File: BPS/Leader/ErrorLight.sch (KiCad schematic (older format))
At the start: 15 parts, among them J10 ErrorLightConn, Q3 NTR4003NT1G, Q4 VND5N07-E, U12 SI8261ABC-IS

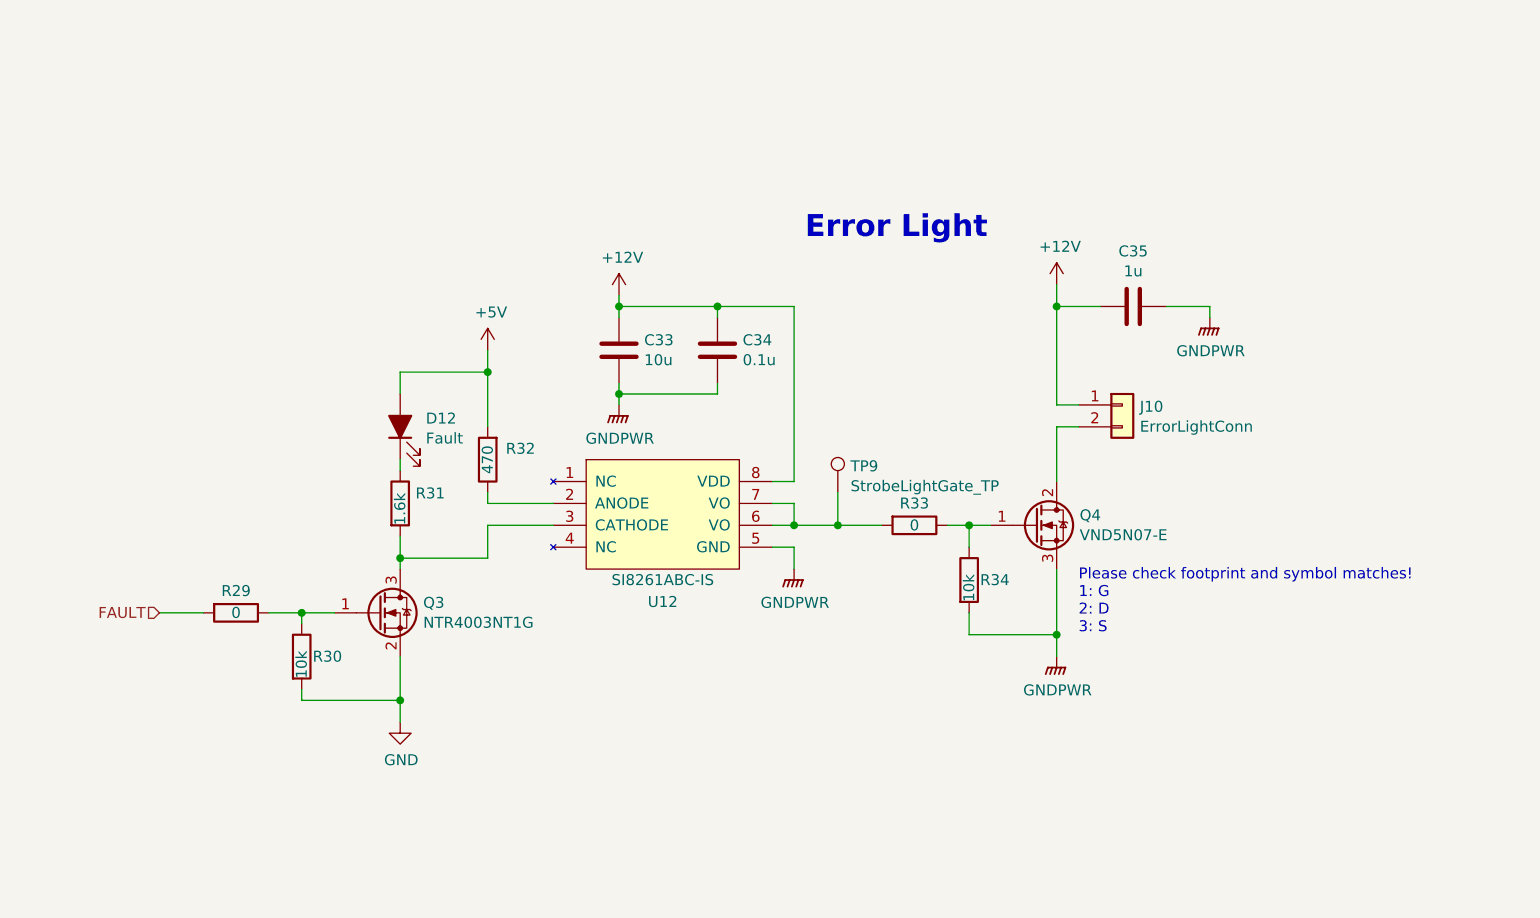
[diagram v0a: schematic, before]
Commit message: Places most components of leader board in their respective locations with nothing traced
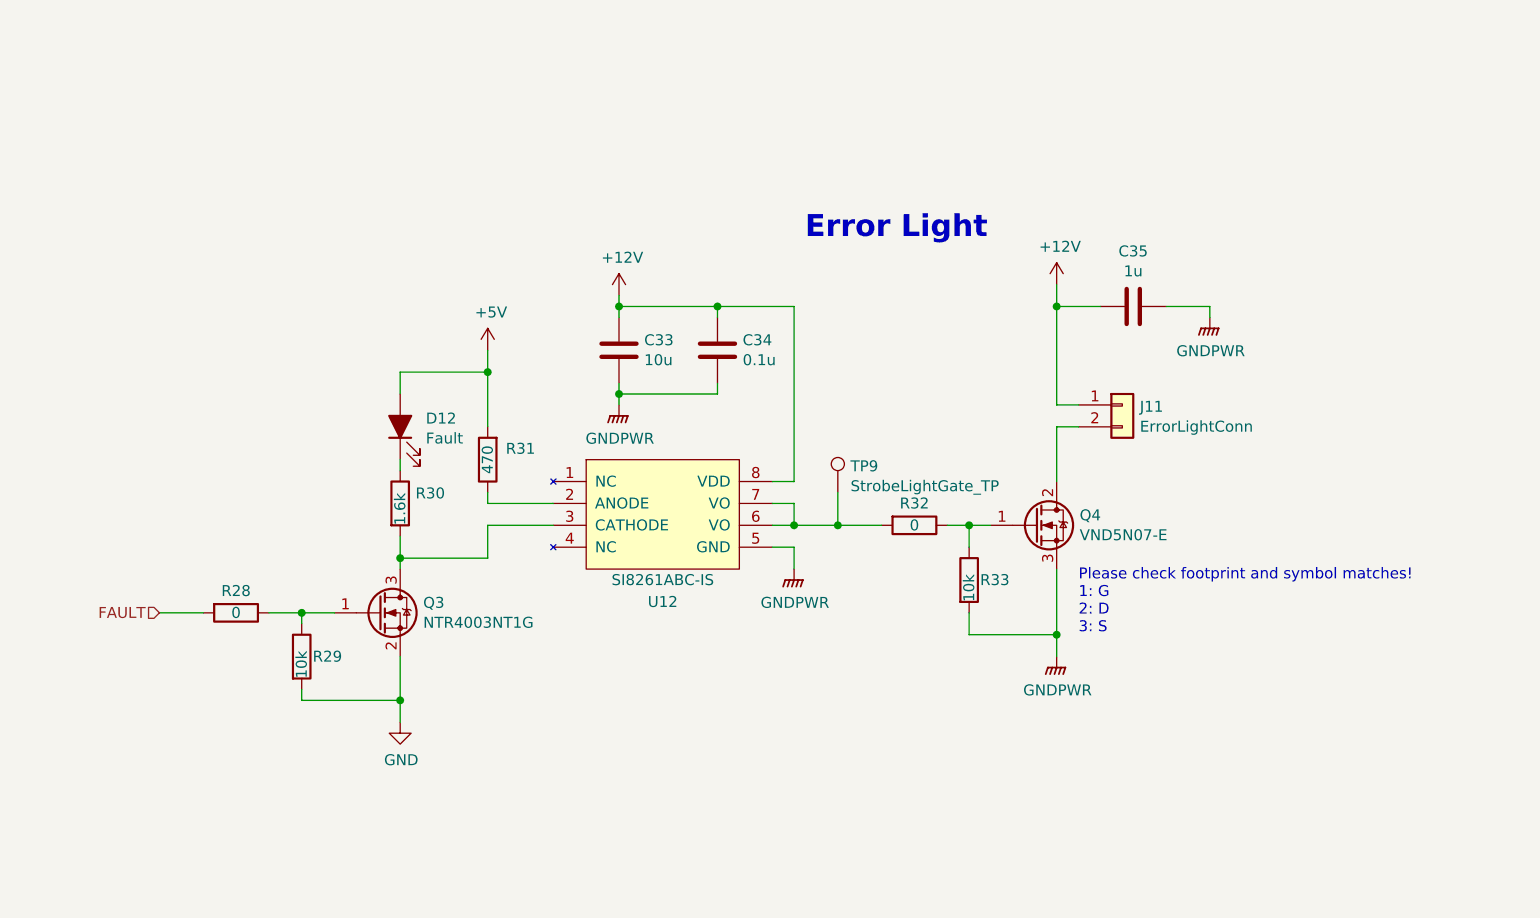
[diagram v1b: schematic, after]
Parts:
- renumbered J10 to J11, R29 to R28, R30 to R29, R31 to R30, R32 to R31, R33 to R32, R34 to R33
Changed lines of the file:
@@
 P 7350 3400
 AR Path="/5C392C6A/5D93093E" Ref="J?"  Part="1"
-AR Path="/5D923D59/5D93093E" Ref="J10"  Part="1"
-F 0 "J10" H 7430 3392 50  0000 L CNN
+AR Path="/5D923D59/5D93093E" Ref="J11"  Part="1"
+F 0 "J11" H 7430 3392 50  0000 L CNN
 F 1 "ErrorLightConn" H 7430 3301 50  0000 L CNN
 F 2 "UTSVT_Connectors:Molex_MicroFit3.0_1x2xP3.00mm_PolarizingPeg_Vertical" H 7350 3400 50  0001 C CNN
@@
 P 4450 3650
 AR Path="/5C392C6A/5D93094B" Ref="R?"  Part="1"
-AR Path="/5D923D59/5D93094B" Ref="R32"  Part="1"
-F 0 "R32" H 4300 3600 50  0000 C CNN
+AR Path="/5D923D59/5D93094B" Ref="R31"  Part="1"
+F 0 "R31" H 4300 3600 50  0000 C CNN
 F 1 "470" V 4450 3650 50  0000 C CNN
 F 2 "Resistor_SMD:R_0805_2012Metric" V 4380 3650 50  0001 C CNN
@@
 AR Path="/5C38C674/5D930988" Ref="R?"  Part="1"
 AR Path="/5C392C6A/5D930988" Ref="R?"  Part="1"
-AR Path="/5D923D59/5D930988" Ref="R34"  Part="1"
-F 0 "R34" H 6700 4200 50  0000 L CNN
+AR Path="/5D923D59/5D930988" Ref="R33"  Part="1"
+F 0 "R33" H 6700 4200 50  0000 L CNN
 F 1 "10k" V 6650 4100 50  0000 L CNN
 F 2 "Resistor_SMD:R_0805_2012Metric" V 6580 4200 50  0001 C CNN
@@
 AR Path="/5C38C674/5D930995" Ref="R?"  Part="1"
 AR Path="/5C392C6A/5D930995" Ref="R?"  Part="1"
-AR Path="/5D923D59/5D930995" Ref="R33"  Part="1"
-F 0 "R33" V 6300 3950 50  0000 C CNN
+AR Path="/5D923D59/5D930995" Ref="R32"  Part="1"
+F 0 "R32" V 6300 3950 50  0000 C CNN
 F 1 "0" V 6400 3950 50  0000 C CNN
 F 2 "Resistor_SMD:R_0805_2012Metric" V 6330 3950 50  0001 C CNN
@@
 AR Path="/5C38C674/5D9309B4" Ref="R?"  Part="1"
 AR Path="/5C392C6A/5D9309B4" Ref="R?"  Part="1"
-AR Path="/5D923D59/5D9309B4" Ref="R31"  Part="1"
-F 0 "R31" H 4120 3896 50  0000 L CNN
+AR Path="/5D923D59/5D9309B4" Ref="R30"  Part="1"
+F 0 "R30" H 4120 3896 50  0000 L CNN
 F 1 "1.6k" V 4050 3750 50  0000 L CNN
 F 2 "Resistor_SMD:R_0805_2012Metric" V 3980 3850 50  0001 C CNN
@@
 AR Path="/5C38C674/5D930A07" Ref="R?"  Part="1"
 AR Path="/5C392C6A/5D930A07" Ref="R?"  Part="1"
-AR Path="/5D923D59/5D930A07" Ref="R29"  Part="1"
-F 0 "R29" V 3200 4350 50  0000 C CNN
+AR Path="/5D923D59/5D930A07" Ref="R28"  Part="1"
+F 0 "R28" V 3200 4350 50  0000 C CNN
 F 1 "0" V 3300 4350 50  0000 C CNN
 F 2 "Resistor_SMD:R_0805_2012Metric" V 3230 4350 50  0001 C CNN
@@
 AR Path="/5C38C674/5D930A0D" Ref="R?"  Part="1"
 AR Path="/5C392C6A/5D930A0D" Ref="R?"  Part="1"
-AR Path="/5D923D59/5D930A0D" Ref="R30"  Part="1"
-F 0 "R30" H 3650 4550 50  0000 L CNN
+AR Path="/5D923D59/5D930A0D" Ref="R29"  Part="1"
+F 0 "R29" H 3650 4550 50  0000 L CNN
 F 1 "10k" V 3600 4450 50  0000 L CNN
 F 2 "Resistor_SMD:R_0805_2012Metric" V 3530 4550 50  0001 C CNN

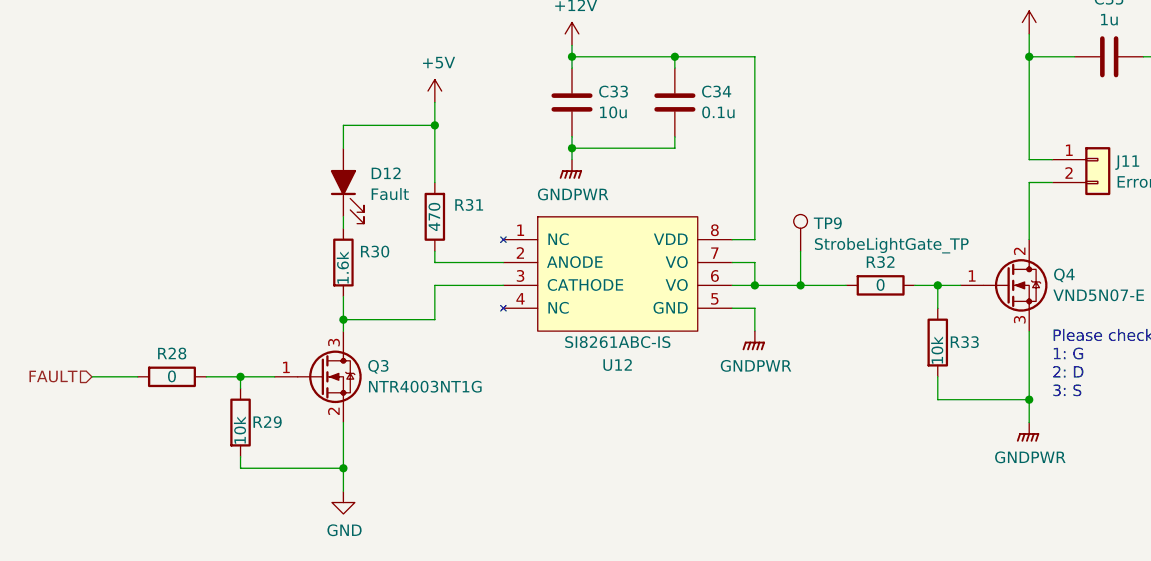
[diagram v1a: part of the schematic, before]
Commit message: Adds power planes
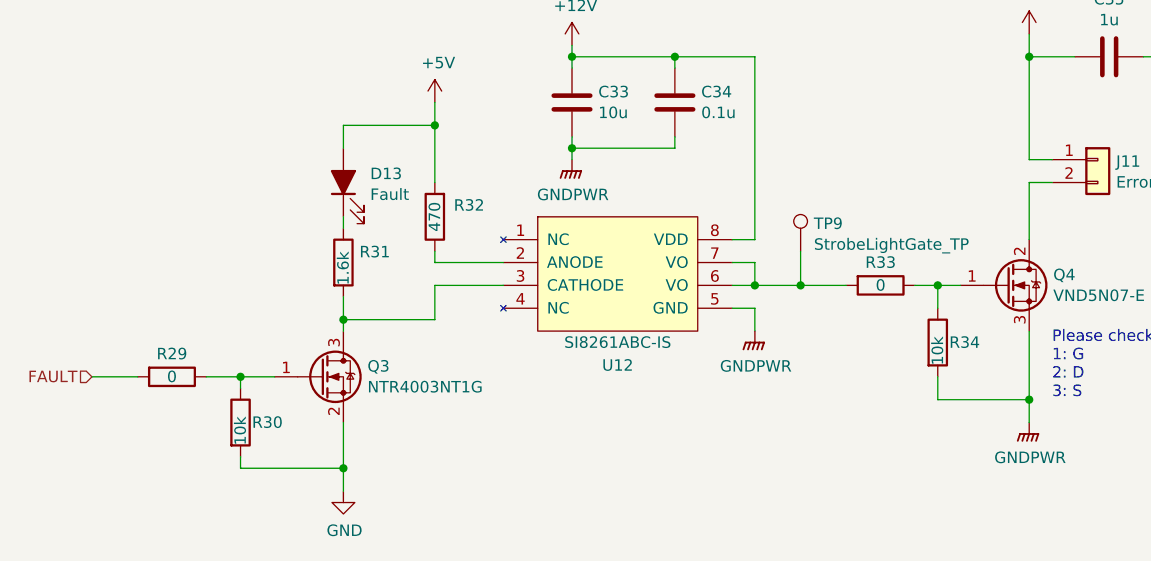
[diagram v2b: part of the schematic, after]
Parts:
- renumbered D12 to D13, R28 to R29, R29 to R30, R30 to R31, R31 to R32, R32 to R33, R33 to R34
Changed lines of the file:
@@
 P 4450 3650
 AR Path="/5C392C6A/5D93094B" Ref="R?"  Part="1"
-AR Path="/5D923D59/5D93094B" Ref="R31"  Part="1"
-F 0 "R31" H 4300 3600 50  0000 C CNN
+AR Path="/5D923D59/5D93094B" Ref="R32"  Part="1"
+F 0 "R32" H 4300 3600 50  0000 C CNN
 F 1 "470" V 4450 3650 50  0000 C CNN
 F 2 "Resistor_SMD:R_0805_2012Metric" V 4380 3650 50  0001 C CNN
@@
 AR Path="/5C38C674/5D930988" Ref="R?"  Part="1"
 AR Path="/5C392C6A/5D930988" Ref="R?"  Part="1"
-AR Path="/5D923D59/5D930988" Ref="R33"  Part="1"
-F 0 "R33" H 6700 4200 50  0000 L CNN
+AR Path="/5D923D59/5D930988" Ref="R34"  Part="1"
+F 0 "R34" H 6700 4200 50  0000 L CNN
 F 1 "10k" V 6650 4100 50  0000 L CNN
 F 2 "Resistor_SMD:R_0805_2012Metric" V 6580 4200 50  0001 C CNN
@@
 AR Path="/5C38C674/5D930995" Ref="R?"  Part="1"
 AR Path="/5C392C6A/5D930995" Ref="R?"  Part="1"
-AR Path="/5D923D59/5D930995" Ref="R32"  Part="1"
-F 0 "R32" V 6300 3950 50  0000 C CNN
+AR Path="/5D923D59/5D930995" Ref="R33"  Part="1"
+F 0 "R33" V 6300 3950 50  0000 C CNN
 F 1 "0" V 6400 3950 50  0000 C CNN
 F 2 "Resistor_SMD:R_0805_2012Metric" V 6330 3950 50  0001 C CNN
@@
 AR Path="/5C38C674/5D9309B4" Ref="R?"  Part="1"
 AR Path="/5C392C6A/5D9309B4" Ref="R?"  Part="1"
-AR Path="/5D923D59/5D9309B4" Ref="R30"  Part="1"
-F 0 "R30" H 4120 3896 50  0000 L CNN
+AR Path="/5D923D59/5D9309B4" Ref="R31"  Part="1"
+F 0 "R31" H 4120 3896 50  0000 L CNN
 F 1 "1.6k" V 4050 3750 50  0000 L CNN
 F 2 "Resistor_SMD:R_0805_2012Metric" V 3980 3850 50  0001 C CNN
@@
 AR Path="/5D9309DA" Ref="D?"  Part="1"
 AR Path="/5C392C6A/5D9309DA" Ref="D?"  Part="1"
-AR Path="/5D923D59/5D9309DA" Ref="D12"  Part="1"
-F 0 "D12" V 4088 3383 50  0000 R CNN
+AR Path="/5D923D59/5D9309DA" Ref="D13"  Part="1"
+F 0 "D13" V 4088 3383 50  0000 R CNN
 F 1 "Fault" V 3997 3383 50  0000 R CNN
 F 2 "LED_SMD:LED_0805_2012Metric" H 4050 3500 50  0001 C CNN
@@
 AR Path="/5C38C674/5D930A07" Ref="R?"  Part="1"
 AR Path="/5C392C6A/5D930A07" Ref="R?"  Part="1"
-AR Path="/5D923D59/5D930A07" Ref="R28"  Part="1"
-F 0 "R28" V 3200 4350 50  0000 C CNN
+AR Path="/5D923D59/5D930A07" Ref="R29"  Part="1"
+F 0 "R29" V 3200 4350 50  0000 C CNN
 F 1 "0" V 3300 4350 50  0000 C CNN
 F 2 "Resistor_SMD:R_0805_2012Metric" V 3230 4350 50  0001 C CNN
@@
 AR Path="/5C38C674/5D930A0D" Ref="R?"  Part="1"
 AR Path="/5C392C6A/5D930A0D" Ref="R?"  Part="1"
-AR Path="/5D923D59/5D930A0D" Ref="R29"  Part="1"
-F 0 "R29" H 3650 4550 50  0000 L CNN
+AR Path="/5D923D59/5D930A0D" Ref="R30"  Part="1"
+F 0 "R30" H 3650 4550 50  0000 L CNN
 F 1 "10k" V 3600 4450 50  0000 L CNN
 F 2 "Resistor_SMD:R_0805_2012Metric" V 3530 4550 50  0001 C CNN
